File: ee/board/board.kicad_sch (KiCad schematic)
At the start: 37 parts, among them J1 Lichee_RV_J3, J2 Lichee_RV_J4, J3 USB_A, J4 Conn_01x08_Pin, J5 Conn_01x10_Pin, J6 Conn_Coaxial, SW1 SW_Push, U2 RTL8723DS, U6 USBLC6-2SC6

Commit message: Changed inductor side in R0.1 to fit the part number.
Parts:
- J4: MPN (none) -> PH1RB-08-UA
- J5: MPN (none) -> PH1RB-10-UA
- J6: MPN (none) -> 901-143-6RFX
- JP1, JP2, JP3: now left out of the parts list
- L2: footprint Inductor_SMD:L_0805_2012Metric -> Resistor_SMD:R_0805_2012Metric
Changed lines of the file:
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@@
+      (effects (font (size 1.27 1.27)) hide)
+    )
+    (property "MPN" "PH1RB-10-UA" (at 194.945 158.75 90)
       (effects (font (size 1.27 1.27)) hide)
     )
@@
       (effects (font (size 1.27 1.27)))
     )
-    (property "Footprint" "Inductor_SMD:L_0805_2012Metric" (at 144.145 172.72 0)
+    (property "Footprint" "Resistor_SMD:R_0805_2012Metric" (at 144.145 172.72 0)
       (effects (font (size 1.27 1.27)) hide)
     )
@@
     )
     (property "Datasheet" " ~" (at 22.86 163.83 0)
+      (effects (font (size 1.27 1.27)) hide)
+    )
+    (property "MPN" "901-143-6RFX" (at 22.86 163.83 0)
       (effects (font (size 1.27 1.27)) hide)
     )
@@
   )
   (symbol (lib_id "Jumper:SolderJumper_2_Bridged") (at 162.56 24.765 0) (unit 1)
-    (in_bom yes) (on_board yes) (dnp no)
+    (in_bom no) (on_board yes) (dnp no)
     (property "Reference" "JP2" (at 162.56 22.225 0)
       (effects (font (size 1.27 1.27)))
@@
   )
   (symbol (lib_id "Jumper:SolderJumper_2_Bridged") (at 117.475 152.4 0) (unit 1)
-    (in_bom yes) (on_board yes) (dnp no)
+    (in_bom no) (on_board yes) (dnp no)
     (property "Reference" "JP1" (at 117.475 149.86 0)
       (effects (font (size 1.27 1.27)))
@@
       (effects (font (size 1.27 1.27)) hide)
     )
+    (property "MPN" "PH1RB-08-UA" (at 158.115 158.75 90)
+      (effects (font (size 1.27 1.27)) hide)
+    )
     (pin "1")
     (pin "2")
@@
   )
   (symbol (lib_id "Jumper:SolderJumper_2_Bridged") (at 162.56 27.305 0) (mirror x) (unit 1)
-    (in_bom yes) (on_board yes) (dnp no)
+    (in_bom no) (on_board yes) (dnp no)
     (property "Reference" "JP3" (at 162.56 29.845 0)
       (effects (font (size 1.27 1.27)))

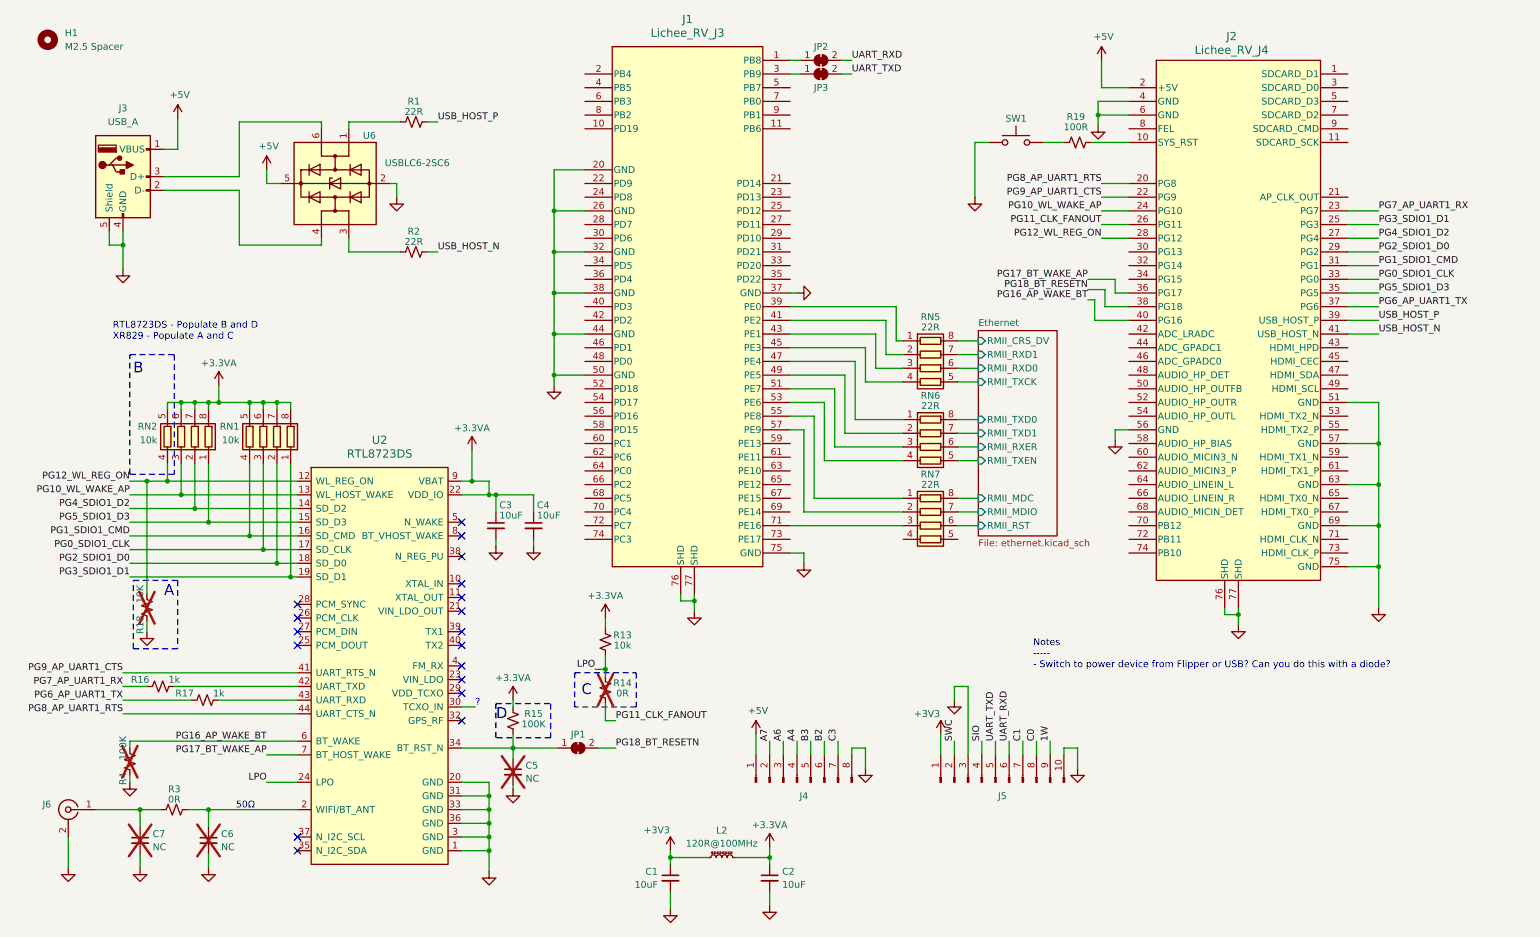
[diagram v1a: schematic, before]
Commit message: Moved to a chip scale
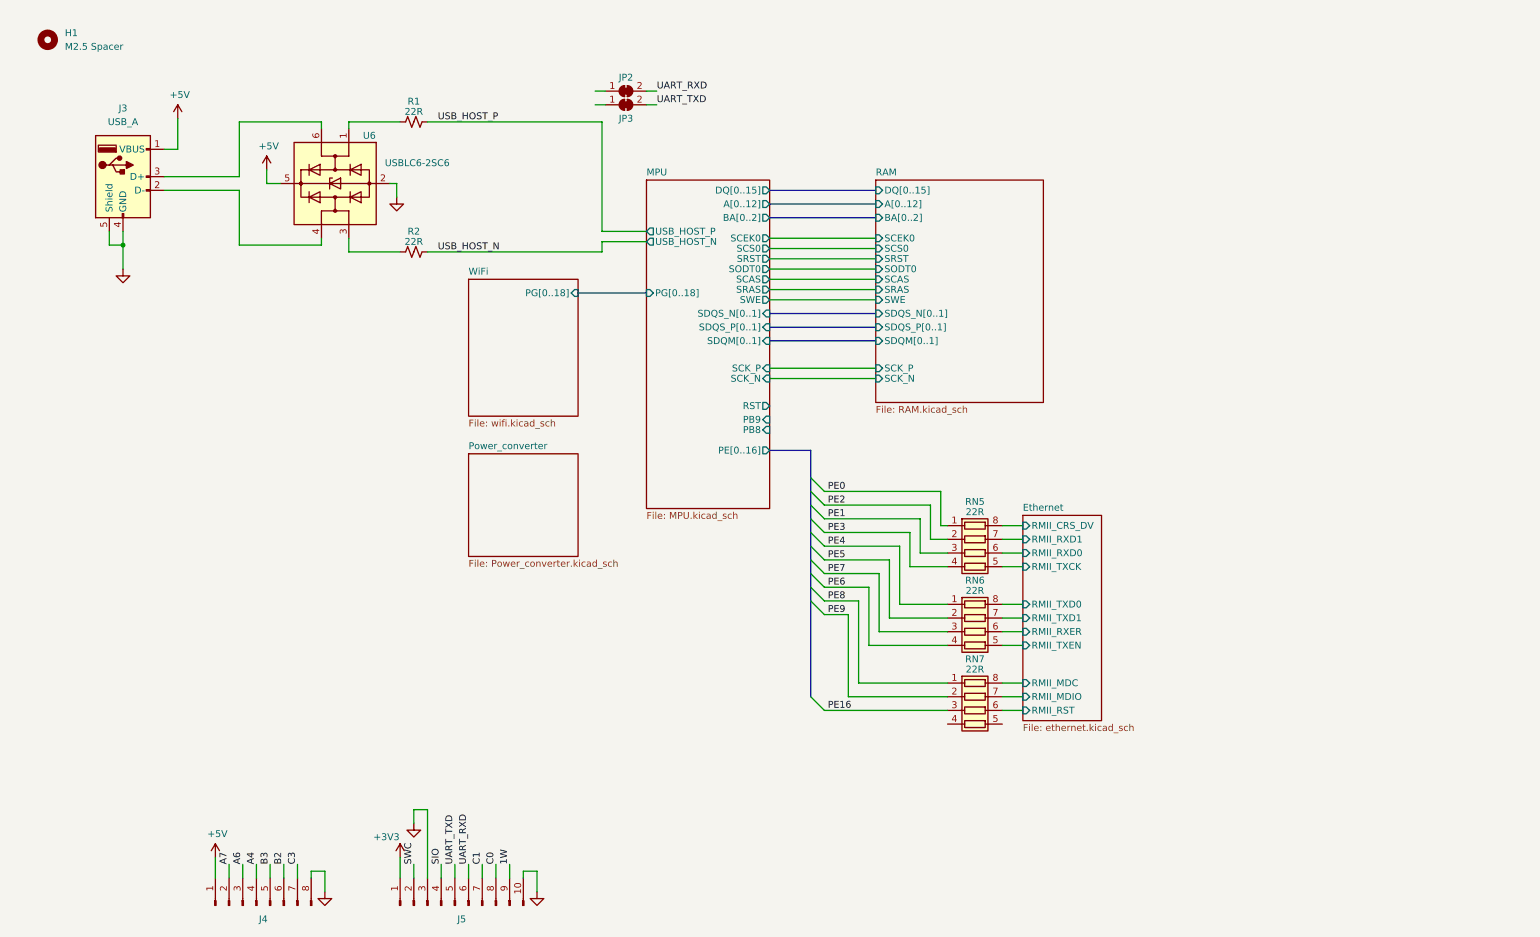
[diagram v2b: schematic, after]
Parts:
- removed C1, C2, C3, C4: 10uF, Capacitor_SMD:C_0603_1608Metric, symbol Device:C_Small
- removed C5, C6, C7: NC, Capacitor_SMD:C_0603_1608Metric, symbol Device:C_Small
- removed J1: Lichee_RV_J3, KiLib:CONN75_2199230-3, symbol lichee_rv_m2:Lichee_RV_J3
- removed J2: Lichee_RV_J4, KiLib:CONN75_2199230-3, symbol lichee_rv_m2:Lichee_RV_J4
- removed J6: Conn_Coaxial, Connector_Coaxial:SMA_Amphenol_901-143_Horizontal, symbol Connector:Conn_Coaxial
- removed JP1: SolderJumper_2_Bridged, Jumper:SolderJumper-2_P1.3mm_Bridged2Bar_RoundedPad1.0x1.5mm, symbol Jumper:SolderJumper_2_Bridged
- removed L2: 120R@100MHz, Resistor_SMD:R_0805_2012Metric, symbol Device:L_Ferrite_Small
- removed R13: 10k, Resistor_SMD:R_0603_1608Metric, symbol Device:R_Small_US
- removed R14, R3: 0R, Resistor_SMD:R_0603_1608Metric, symbol Device:R_Small_US
- removed R15, R4: 100K, Resistor_SMD:R_0603_1608Metric, symbol Device:R_Small_US
- removed R16, R17: 1k, Resistor_SMD:R_0603_1608Metric, symbol Device:R_Small_US
- removed R18: 10K, Resistor_SMD:R_0603_1608Metric, symbol Device:R_Small_US
- removed R19: 100R, Resistor_SMD:R_0603_1608Metric, symbol Device:R_Small_US
- removed RN1, RN2: 10k, Resistor_SMD:R_Array_Convex_4x0402, symbol Device:R_Pack04
- removed SW1: SW_Push, Button_Switch_SMD:SW_SPST_PTS645, symbol Switch:SW_Push
- removed U2: RTL8723DS, KiLib:RTL8723, symbol rtl8723ds:RTL8723DS
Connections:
- net PE4: now reaches RN6.1 (R1.1)
- net PE5: now reaches RN6.2 (R2.1)
- net PE7: now reaches RN6.3 (R3.1)
- net PE6: now reaches RN6.4 (R4.1)
- net PE0: now reaches RN5.1 (R1.1)
- net PE2: now reaches RN5.2 (R2.1)
- net PE1: now reaches RN5.3 (R3.1)
- net PE3: now reaches RN5.4 (R4.1)
- net PE8: now reaches RN7.1 (R1.1)
- net PE9: now reaches RN7.2 (R2.1)
- net PE16: now reaches RN7.3 (R3.1)
- no-connect marks 18 -> 0
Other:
- added sheet MPU (MPU.kicad_sch)
- added sheet Power_converter (Power_converter.kicad_sch)
- added sheet RAM (RAM.kicad_sch)
- added sheet WiFi (wifi.kicad_sch)
- note removed: "50Ω"
- note removed: "?"
- note removed: "A"
- note removed: "B"
- note removed: "C"
- note removed: "D"
- note removed: "Notes ----- - Switch to power device from Flipper or USB? Can you do this with a diode?"
- note removed: "RTL8723DS - Populate B and D XR829 - Populate A and C"
- moved on the sheet: J4, J5, JP2, JP3, RN5, RN6, RN7

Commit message: Added the footprints into the design.
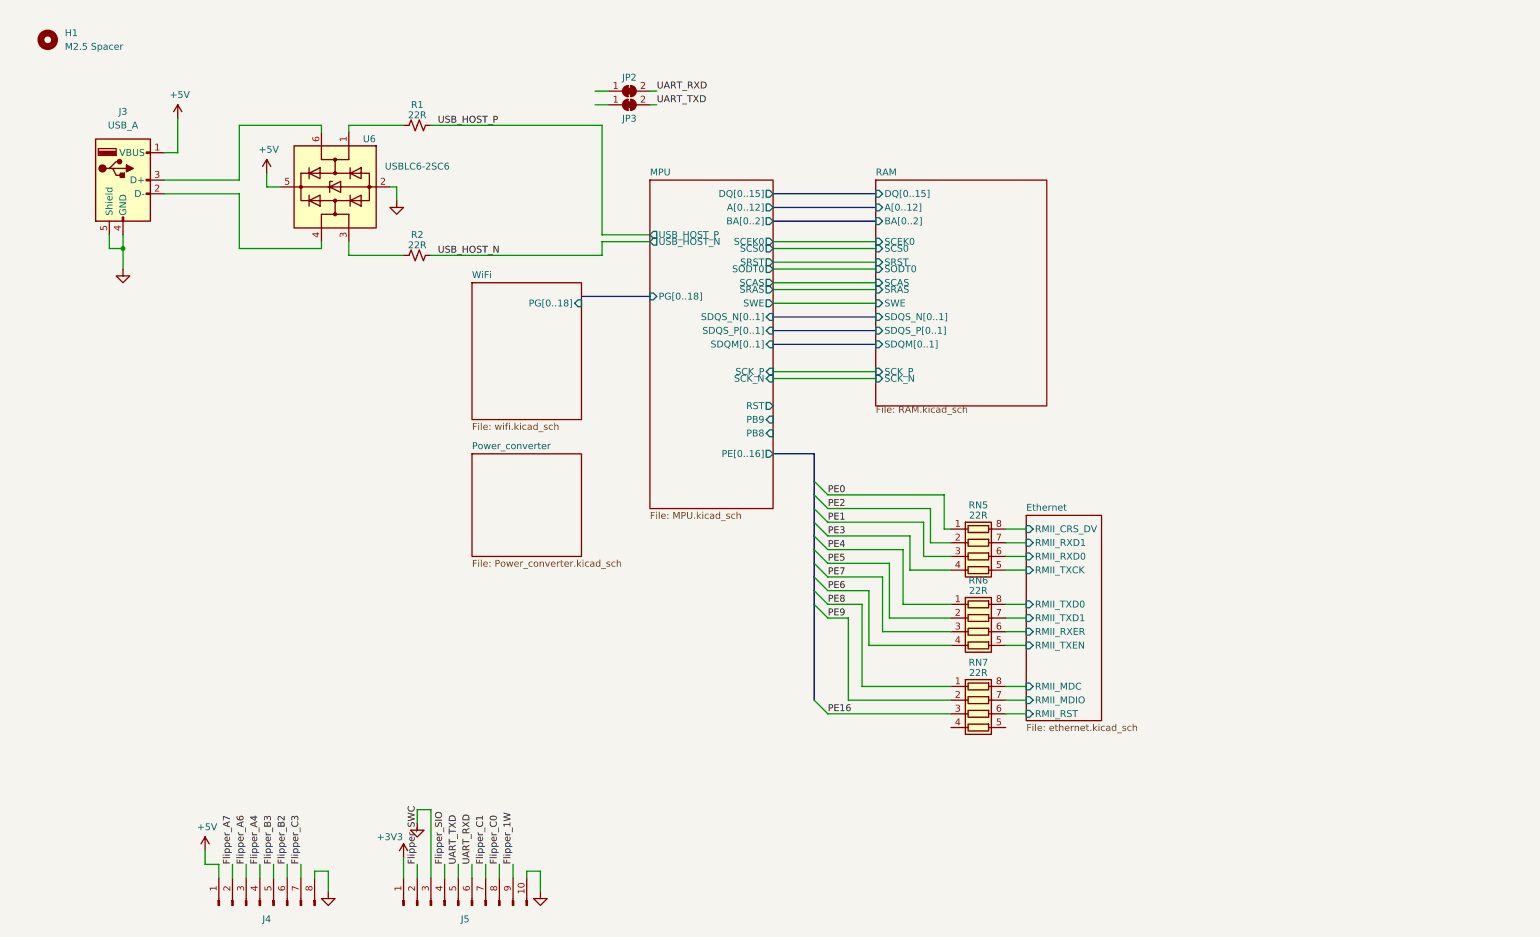
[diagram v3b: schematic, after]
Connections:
- net 1W renamed Flipper_1W
- net A4 renamed Flipper_A4
- net A6 renamed Flipper_A6
- net A7 renamed Flipper_A7
- net B2 renamed Flipper_B2
- net B3 renamed Flipper_B3
- net C0 renamed Flipper_C0
- net C1 renamed Flipper_C1
- net C3 renamed Flipper_C3
- net SIO renamed Flipper_SIO
- net SWC renamed Flipper_SWC
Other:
- moved on the sheet: J3, J4, J5, JP2, JP3, R1, R2, RN5, RN6, RN7, U6
